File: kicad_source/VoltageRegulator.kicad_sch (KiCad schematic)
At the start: 40 parts, among them J10 x, J11 PowerPole, J12 Conn_01x02, Q2 IPD90P04P4L- 04, U12 INA226, U13 IFX91041EFJ

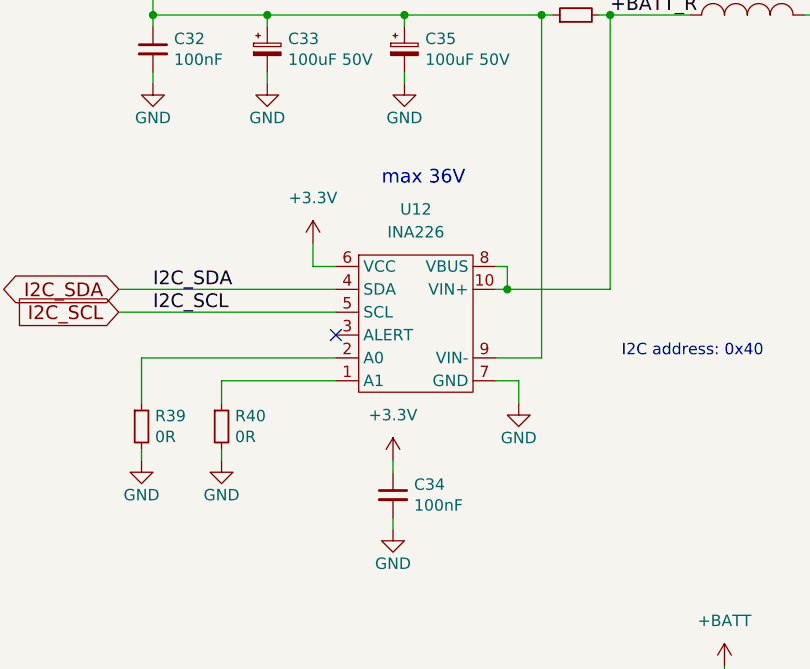
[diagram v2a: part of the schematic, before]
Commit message: replaced INA226 by INA232 to support up to 40V
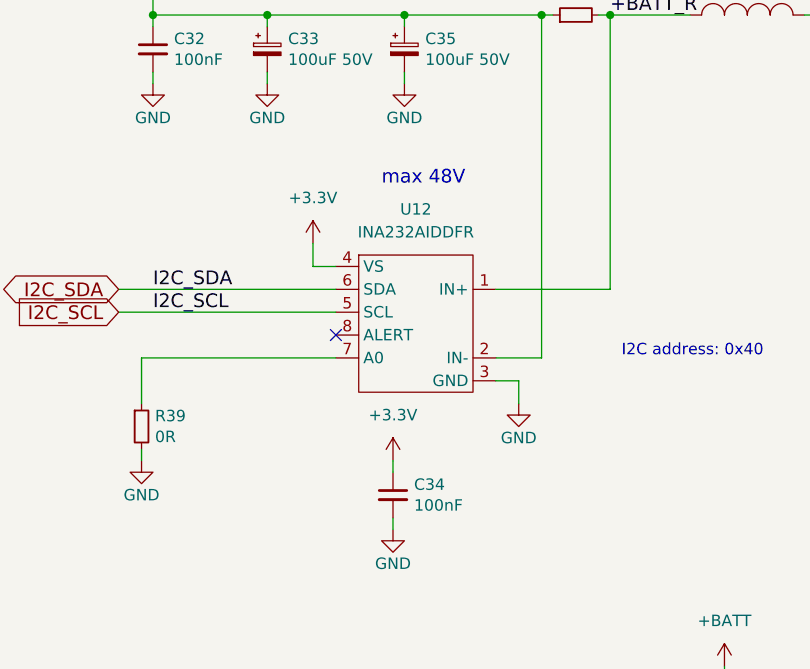
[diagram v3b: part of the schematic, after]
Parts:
- removed R40: 0R, Resistor_SMD:R_0603_1608Metric, symbol Device:R_Small
- U12: value INA226 -> INA232AIDDFR; footprint Package_SO:MSOP-10_3x3mm_P0.5mm -> Package_TO_SOT_SMD:SOT-23-8; symbol generationmake:INA226 -> generationmake:INA232
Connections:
- net +3.3V: now also U12.4 (VS); no longer U12.6 (VCC)
- net +BATT: now also U12.2 (IN-); no longer U12.9 (VIN-)
- net +BATT_R: now also U12.1 (IN+); no longer U12.10 (VIN+), U12.8 (VBUS)
- net GND: now also U12.3 (GND); no longer U12.7 (GND)
- net I2C_SDA: now also U12.6 (SDA); no longer U12.4 (SDA)
- net at R39.1: now also U12.7 (A0); no longer U12.2 (A0)
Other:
- note added: "max 48V"
- note removed: "max 36V"
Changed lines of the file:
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@@
   (junction (at 143.51 135.89) (diameter 0) (color 0 0 0 0)
-  )
-  (junction (at 87.63 59.69) (diameter 0) (color 0 0 0 0)
   )
   (junction (at 161.29 29.21) (diameter 0) (color 0 0 0 0)
@@
     (stroke (width 0) (type default) (color 0 0 0 0))
   )
-  (wire (pts (xy 86.36 57.15) (xy 87.63 57.15))
-    (stroke (width 0) (type default) (color 0 0 0 0))
-  )
   (wire (pts (xy 44.45 62.23) (xy 68.58 62.23))
     (stroke (width 0) (type default) (color 0 0 0 0))
@@
     (stroke (width 0) (type default) (color 0 0 0 0))
   )
-  (wire (pts (xy 87.63 57.15) (xy 87.63 59.69))
-    (stroke (width 0) (type default) (color 0 0 0 0))
-  )
   (wire (pts (xy 189.23 44.45) (xy 187.96 44.45))
     (stroke (width 0) (type default) (color 0 0 0 0))
@@
     (stroke (width 0) (type default) (color 0 0 0 0))
   )
-  (wire (pts (xy 55.88 77.47) (xy 55.88 78.74))
-    (stroke (width 0) (type default) (color 0 0 0 0))
-  )
   (wire (pts (xy 130.81 110.49) (xy 130.81 111.76))
     (stroke (width 0) (type default) (color 0 0 0 0))
@@
     (stroke (width 0) (type default) (color 0 0 0 0))
   )
-  (wire (pts (xy 87.63 59.69) (xy 99.06 59.69))
-    (stroke (width 0) (type default) (color 0 0 0 0))
-  )
   (wire (pts (xy 99.06 59.69) (xy 99.06 29.21))
     (stroke (width 0) (type default) (color 0 0 0 0))
@@
     (stroke (width 0) (type default) (color 0 0 0 0))
   )
-  (wire (pts (xy 55.88 69.85) (xy 55.88 72.39))
-    (stroke (width 0) (type default) (color 0 0 0 0))
-  )
   (wire (pts (xy 48.26 29.21) (xy 48.26 26.67))
     (stroke (width 0) (type default) (color 0 0 0 0))
@@
     (stroke (width 0) (type default) (color 0 0 0 0))
   )
-  (wire (pts (xy 86.36 59.69) (xy 87.63 59.69))
+  (wire (pts (xy 86.36 59.69) (xy 99.06 59.69))
     (stroke (width 0) (type default) (color 0 0 0 0))
   )
@@
   )
   (wire (pts (xy 124.46 29.21) (xy 134.62 29.21))
-    (stroke (width 0) (type default) (color 0 0 0 0))
-  )
-  (wire (pts (xy 68.58 69.85) (xy 55.88 69.85))
     (stroke (width 0) (type default) (color 0 0 0 0))
   )
@@
     (effects (font (size 1.524 1.524)) (justify left bottom))
   )
-  (text "max 36V" (at 73.66 48.26 0)
+  (text "max 48V" (at 73.66 48.26 0)
     (effects (font (size 1.524 1.524)) (justify left bottom))
   )
@@
     (pin "1")
   )
-  (symbol (lib_id "Device:R_Small") (at 55.88 74.93 0) (unit 1)
-    (in_bom yes) (on_board yes)
-    (property "Reference" "R40" (id 0) (at 57.3786 73.7616 0)
-      (effects (font (size 1.27 1.27)) (justify left))
-    )
-    (property "Value" "0R" (id 1) (at 57.3786 76.073 0)
-      (effects (font (size 1.27 1.27)) (justify left))
-    )
-    (property "Footprint" "Resistor_SMD:R_0603_1608Metric" (id 2) (at 55.88 78.74 0)
-      (effects (font (size 1.27 1.27)) hide)
-    )
-    (property "Datasheet" "" (id 3) (at 55.88 74.93 0))
-    (pin "1")
-    (pin "2")
-  )
   (symbol (lib_id "Device:Fuse_Small") (at 165.1 29.21 0) (unit 1)
     (in_bom yes) (on_board yes) (fields_autoplaced)
@@
     (pin "2")
   )
-  (symbol (lib_id "generationmake:INA226") (at 77.47 63.5 0) (unit 1)
+  (symbol (lib_id "generationmake:INA232") (at 77.47 63.5 0) (unit 1)
     (in_bom yes) (on_board yes) (fields_autoplaced)
     (property "Reference" "U12" (id 0) (at 77.47 50.8 0))
-    (property "Value" "INA226" (id 1) (at 77.47 53.34 0))
-    (property "Footprint" "Package_SO:MSOP-10_3x3mm_P0.5mm" (id 2) (at 77.47 63.5 0)
+    (property "Value" "INA232AIDDFR" (id 1) (at 77.47 53.34 0))
+    (property "Footprint" "Package_TO_SOT_SMD:SOT-23-8" (id 2) (at 77.47 63.5 0)
       (effects (font (size 1.27 1.27)) hide)
     )
@@
     )
     (pin "1")
-    (pin "10")
     (pin "2")
     (pin "3")
@@
     (pin "7")
     (pin "8")
-    (pin "9")
   )
   (symbol (lib_id "power:+5V") (at 255.27 92.71 0) (unit 1)
@@
     (pin "2")
   )
-  (symbol (lib_id "power:GND") (at 55.88 78.74 0) (unit 1)
-    (in_bom yes) (on_board yes)
-    (property "Reference" "#PWR098" (id 0) (at 55.88 85.09 0)
-      (effects (font (size 1.27 1.27)) hide)
-    )
-    (property "Value" "GND" (id 1) (at 55.88 82.55 0))
-    (property "Footprint" "" (id 2) (at 55.88 78.74 0))
-    (property "Datasheet" "" (id 3) (at 55.88 78.74 0))
-    (pin "1")
-  )
   (symbol (lib_id "Device:C_Small") (at 149.86 33.02 0) (unit 1)

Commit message: beautified layout
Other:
- note added: "max 1.8A"
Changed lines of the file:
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@@
     (effects (font (size 1.27 1.27)) (justify left bottom))
+  )
+  (text "max 1.8A" (at 243.84 114.3 0)
+    (effects (font (size 1.524 1.524)) (justify left bottom))
   )
   (text "measure up to +- 8.192 A" (at 78.74 19.05 0)
